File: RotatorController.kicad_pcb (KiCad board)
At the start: 2 copper layers, 117 x 94 mm, 60 parts, among them J1 USB_A, J2 26 VAC, J3 Rotator, K1 G5LE-1, K2 G5LE-1, K3 G5LE-1, Q1 BSS123, Q2 BSS123, Q3 BSS123, SW1 SW_CW, SW2 SW_CCW, U1 Teensy4.0, U3 AP2161W

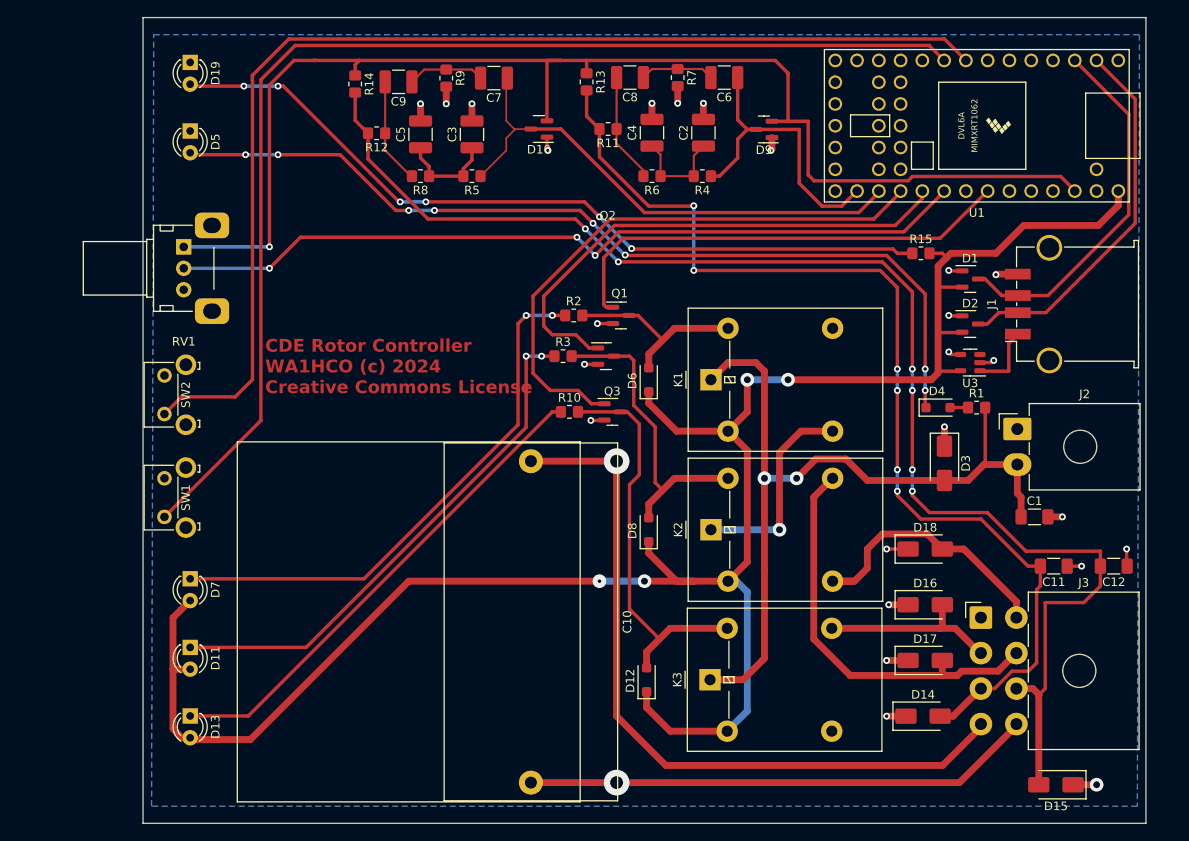
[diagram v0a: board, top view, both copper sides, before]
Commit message: Added files Update board outline based on measurements Moved connectors to new board outline
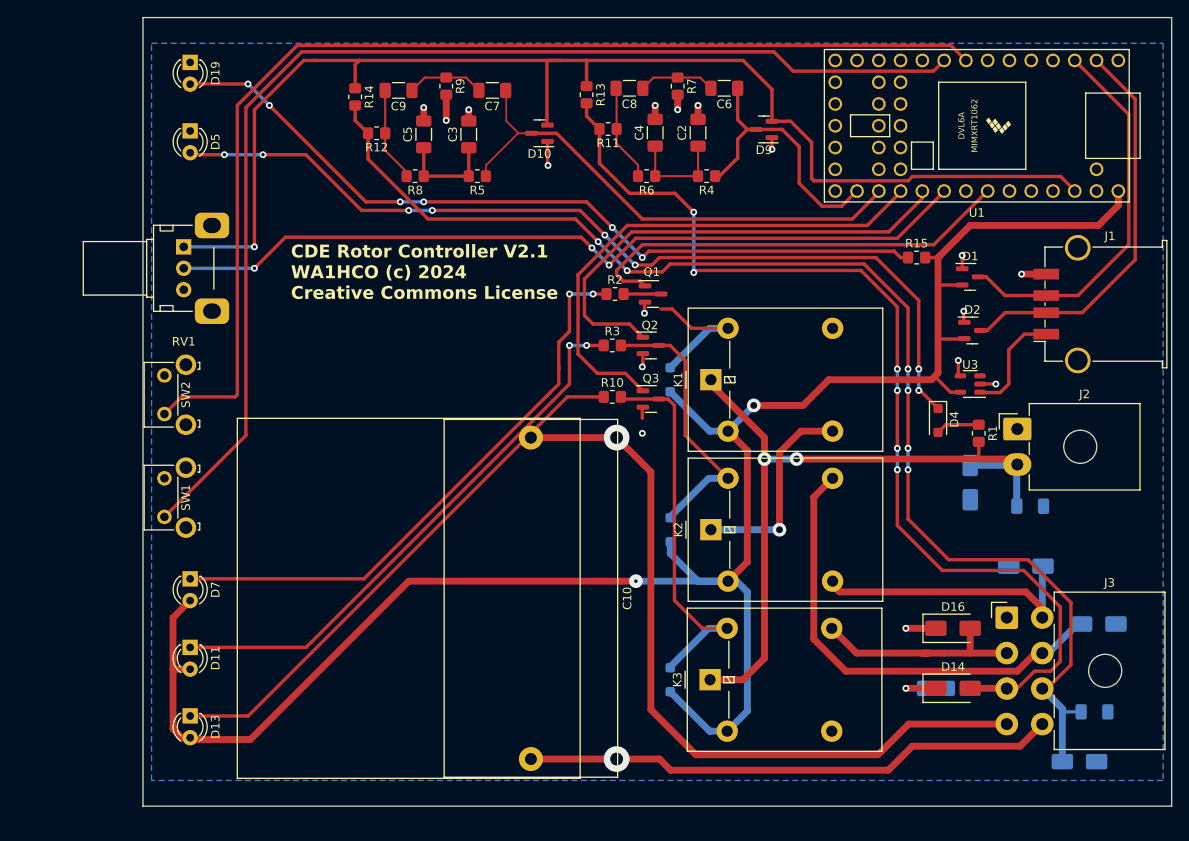
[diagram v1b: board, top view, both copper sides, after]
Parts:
- C1, C11, C12, D12, D15, D17, D18, D3, D6, D8: moved to B.Cu
- C2, C3, C4, C5, C6, C7, C8, C9: footprint Capacitor_SMD:C_1210_3225Metric_Pad1.33x2.70mm_HandSolder -> Capacitor_SMD:C_1206_3216Metric_Pad1.33x1.80mm_HandSolder
- moved D17 20.7 mm to (206.2, 117.8), turned to 180 degrees
- moved C11 19.8 mm to (187.2, 125.2), turned to 0 degrees
- moved C12 17.1 mm to (205.8, 128.0)
- moved D18 11.9 mm to (197.8, 111.0)
- moved R3 5.88 mm to (149.5, 85.2)
- moved R2 5.42 mm to (149.8, 79.2)
- moved Q2 5.40 mm to (154.0, 85.2)
- moved R10 5.30 mm to (149.5, 91.2)
- moved D14 4.78 mm to (189.2, 125.2)
- moved Q3 4.74 mm to (154.0, 91.5)
- moved Q1 4.51 mm to (154.2, 79.2)
- moved D16 4.26 mm to (189.2, 118.2)
- moved D15 3.85 mm to (204.0, 133.8)
- moved D3 3.75 mm to (191.2, 101.2), turned to 90 degrees
- moved J1 3.31 mm to (206.5, 80.4)
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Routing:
- net /Wiper-: track 162.5 -> 148.9 mm
- net GND: track 48.7 -> 35.8 mm, vias 25 -> 18
- net /26VAC: track 94.0 -> 84.7 mm
- net /Right: track 47.9 -> 54.7 mm
- net /Brk_Ctl: track 66.9 -> 60.4 mm
- net /+5V: track 240.5 -> 234.3 mm, vias 4 -> 2
- net Net-(D13-K): track 57.9 -> 63.7 mm
- net Net-(J1-VBUS): track 8.14 -> 12.9 mm
- net Net-(D7-K): track 63.4 -> 68.0 mm
- net /Dir_Ctl: track 61.1 -> 56.7 mm
- net /Brake: track 21.2 -> 25.4 mm
- net Net-(D11-K): track 61.4 -> 65.5 mm
- net /Wiper+: track 124.3 -> 120.3 mm
- net Net-(D8-A): track 36.1 -> 32.8 mm
- net Net-(D4-A): track 2.10 -> 5.12 mm
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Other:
- board size 117 x 94 mm -> 120 x 92 mm
- board text added: "CDE Rotor Controller V2.1 WA1HCO (c) 2024 Creative Commons License"
- board text removed: "CDE Rotor Controller WA1HCO (c) 2024 Creative Commons License"

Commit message: Moved Teensy into position, adjusted related traces
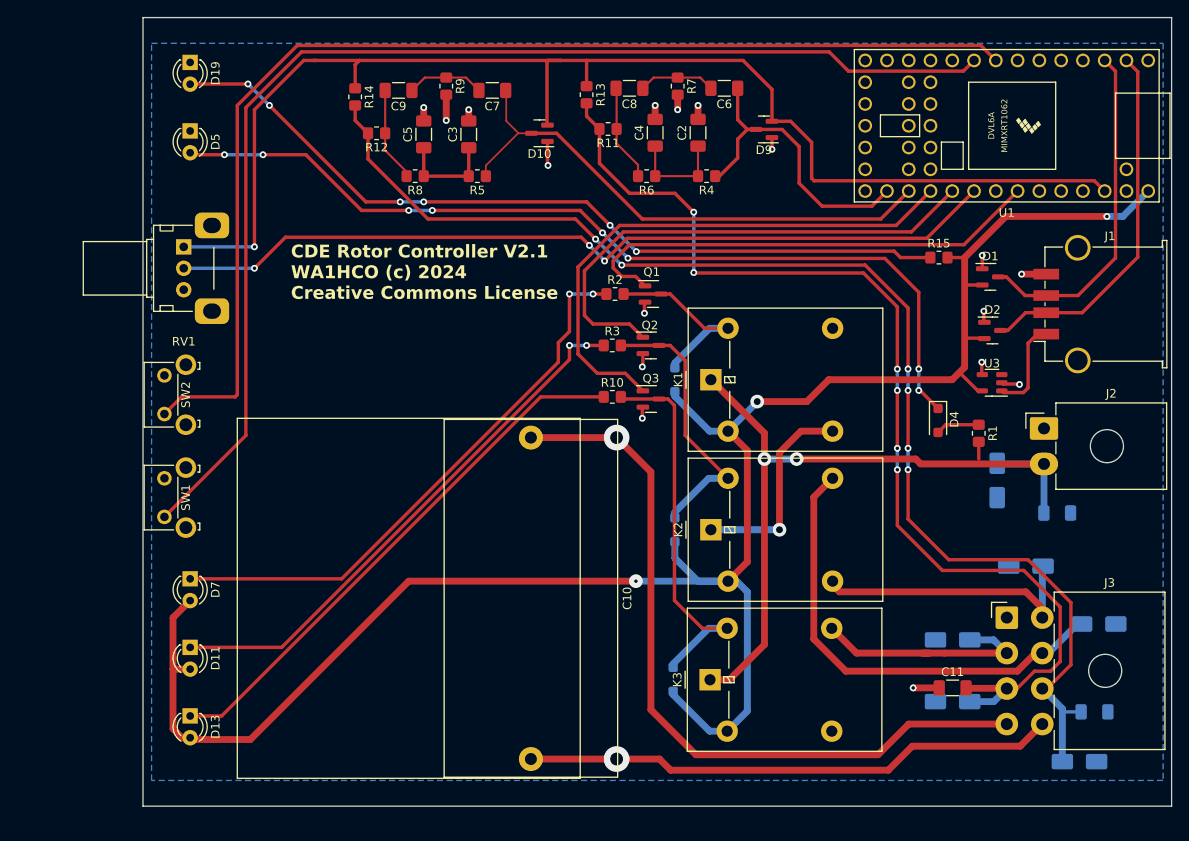
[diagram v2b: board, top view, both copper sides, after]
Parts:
- C11: moved to F.Cu
- D14, D16: moved to B.Cu
- moved U1 3.49 mm to (195.5, 59.6)
- moved C1 3.25 mm to (201.4, 104.8)
- moved D3 3.16 mm to (194.4, 101.0)
- moved J2 3.11 mm to (199.9, 94.9)
- moved R15 2.60 mm to (187.6, 75.0)
- moved U3 2.55 mm to (193.8, 89.6)
- moved D1 2.34 mm to (193.6, 77.2)
- moved D2 2.34 mm to (193.8, 83.5)
- moved C11 1.95 mm to (189.2, 125.2)
- moved D14 1.55 mm to (189.2, 126.8)
- moved D16 1.35 mm to (189.2, 119.6)
- moved D6 0.55 mm to (156.8, 89.2)
- moved D8 0.55 mm to (156.8, 106.8)
- moved D12 0.35 mm to (156.6, 124.2)
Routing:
- net /Wiper+: track 120.3 -> 125.5 mm
- net /Ctlr_Tx: track 45.0 -> 40.0 mm
- net /Mot_Ctl: track 51.7 -> 56.2 mm
- net GND: track 35.8 -> 31.6 mm, vias 18 -> 17
- net /Brk_Ctl: track 60.4 -> 64.3 mm
- net /Ctlr_Rx: track 46.6 -> 43.1 mm
- net /Flt_W+: track 32.3 -> 35.8 mm
- net /CW: track 137.3 -> 140.8 mm
- net /CCW: track 131.8 -> 135.3 mm
- net /Dir_Ctl: track 56.7 -> 59.8 mm
- net /Hdg: track 95.2 -> 98.3 mm
- net /3V3: track 149.7 -> 152.7 mm
- net /26VAC: track 84.7 -> 87.6 mm
- net /Flt_W-: track 60.5 -> 63.2 mm
- net /Brake: track 25.4 -> 27.4 mm
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
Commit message: Mid layout of smaller pcb with separately mounted cap still need to assign cap connector Added 4 high light pipe and 0805 LEDs, need to create footprint
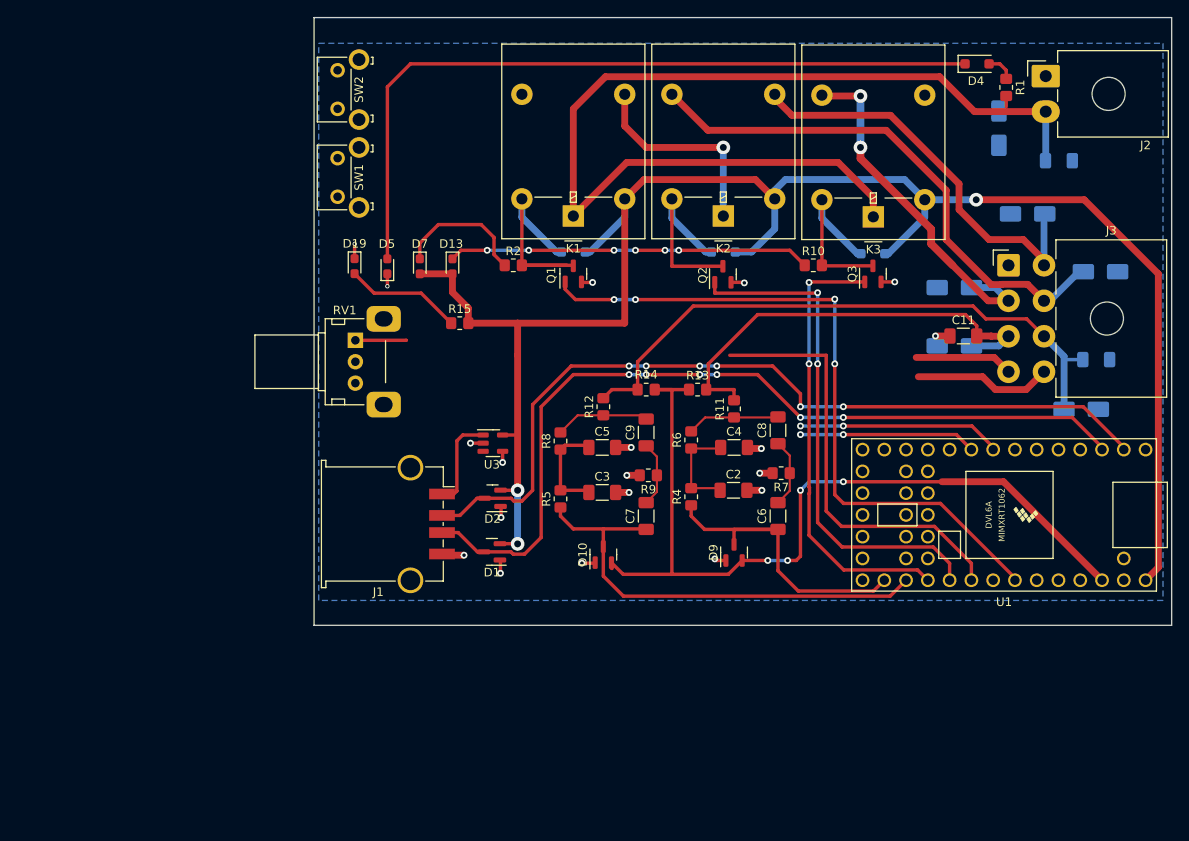
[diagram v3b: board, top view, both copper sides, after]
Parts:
- removed C10: 100 uFd, Capacitor_THT:C_Rect_L41.5mm_W20.0mm_P37.50mm_MKS4
- removed D11: IR204A, LED_THT:LED_D3.0mm_IRBlack
- removed R3: 560, Resistor_SMD:R_0805_2012Metric_Pad1.20x1.40mm_HandSolder
- D13: value IR204A -> Brake; footprint LED_THT:LED_D3.0mm_IRBlack -> LED_SMD:LED_0603_1608Metric_Pad1.05x0.95mm_HandSolder
- D19: value IR204A -> 5V; footprint LED_THT:LED_D3.0mm_IRBlack -> LED_SMD:LED_0603_1608Metric_Pad1.05x0.95mm_HandSolder
- D5: value IR204A -> 26VAC; footprint LED_THT:LED_D3.0mm_IRBlack -> LED_SMD:LED_0603_1608Metric_Pad1.05x0.95mm_HandSolder
- D7: value IR204A -> Motor; footprint LED_THT:LED_D3.0mm_IRBlack -> LED_SMD:LED_0603_1608Metric_Pad1.05x0.95mm_HandSolder
- moved J1 87.1 mm to (123.2, 106.1), turned to -90 degrees
- moved D1 66.4 mm to (135.4, 109.3), turned to 180 degrees
- moved D2 61.5 mm to (135.5, 103.1), turned to 180 degrees
- moved D13 60.7 mm to (130.9, 76.0)
- moved U3 58.7 mm to (135.6, 96.7), turned to 0 degrees
- moved K3 57.3 mm to (179.9, 70.2), turned to 180 degrees
- moved R15 56.4 mm to (131.7, 82.7)
- moved D12 54.8 mm to (179.9, 74.5), turned to 180 degrees
- moved C7 52.8 mm to (153.4, 105.2), turned to 90 degrees
- moved R9 51.2 mm to (153.7, 100.4), turned to 180 degrees
- moved C6 50.3 mm to (168.8, 105.2), turned to 90 degrees
- moved D10 49.7 mm to (148.4, 109.7), turned to 90 degrees
- moved D9 49.5 mm to (163.7, 109.4), turned to 90 degrees
- moved C9 49.3 mm to (153.4, 95.4), turned to 90 degrees
- moved R14 48.2 mm to (153.4, 90.4), turned to 180 degrees
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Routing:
- net /CW: track 140.8 -> 20.7 mm, vias 0 -> 2
- net /CCW: track 135.3 -> 23.8 mm, vias 0 -> 2
- net Net-(D19-A): track 94.8 -> 13.7 mm, vias 6 -> 0
- net /Wiper-: track 148.2 -> 70.9 mm, vias 6 -> 0
- net /Cap1: track 88.6 -> 11.5 mm, vias 1 -> 0
- net /Wiper+: track 125.5 -> 51.4 mm, vias 6 -> 0
- net Net-(D11-K): track 63.8 -> 0.00 mm, vias 2 -> 0
- net /Ctlr_Tx: track 40.0 -> 99.4 mm, vias 0 -> 6
- net /Ctlr_Rx: track 43.1 -> 98.0 mm, vias 0 -> 6
- net Net-(D7-K): track 66.2 -> 15.8 mm, vias 2 -> 0
- net /Hdg: track 98.3 -> 50.9 mm, vias 3 -> 0
- net /3V3: track 152.7 -> 106.0 mm, vias 1 -> 4
- net /Cap2: track 62.4 -> 16.1 mm, vias 1 -> 0
- net /26VAC: track 87.6 -> 124.9 mm, vias 2 -> 0
- net /+5V: track 234.7 -> 207.7 mm
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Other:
- board size 120 x 92 mm -> 100 x 70.9 mm

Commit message: Added light pipe footprint Completed layout and deisgn rule check
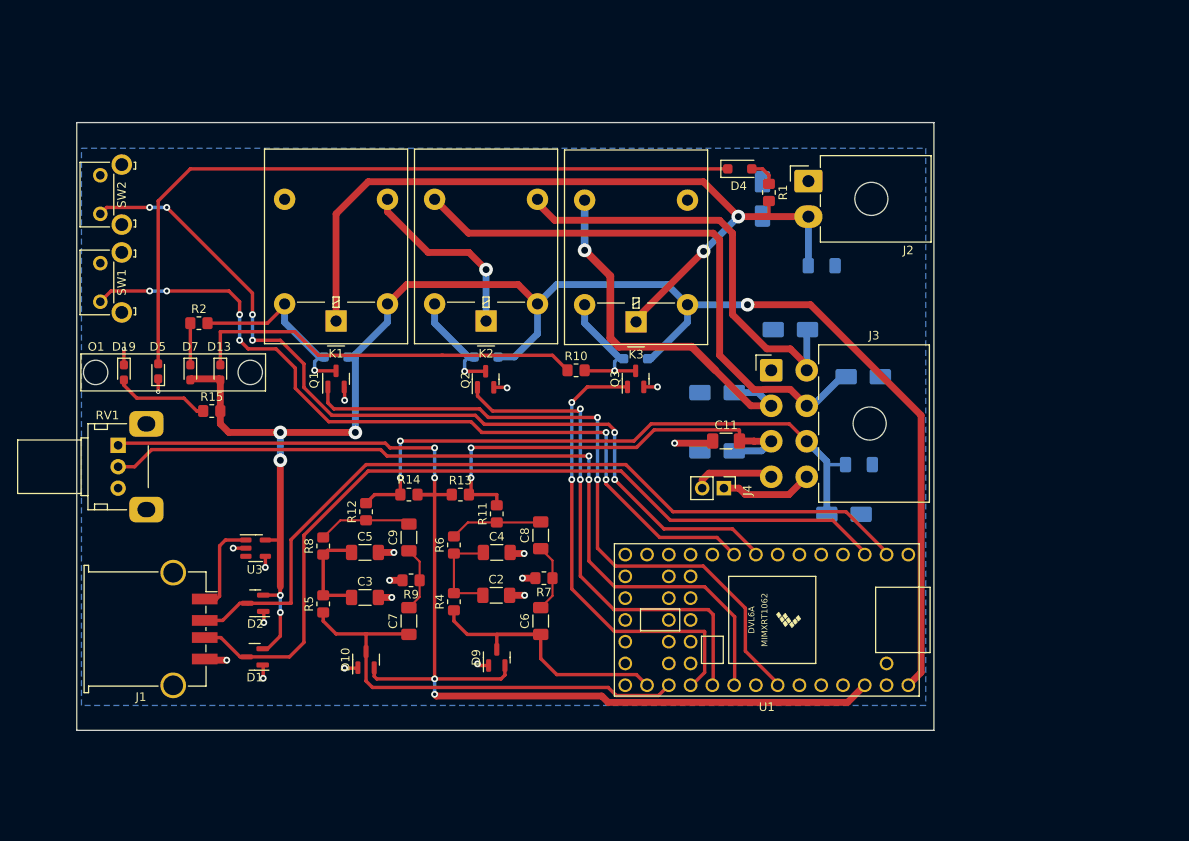
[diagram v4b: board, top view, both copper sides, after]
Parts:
- added J4: Motor Cap, Connector_PinHeader_2.54mm:PinHeader_1x02_P2.54mm_Vertical, F.Cu at (162.5, 101.9)
- added O1: ~, Lightpipe:LP4-EP, F.Cu at (89.2, 88.4)
- moved R2 37.3 mm to (101.3, 82.7)
- moved D18 30.8 mm to (170.3, 83.4)
- moved R15 30.7 mm to (102.8, 92.9)
- moved D4 30.3 mm to (164.4, 64.7)
- moved SW2 30.3 mm to (89.8, 69.9)
- moved RV1 30.3 mm to (91.8, 96.9)
- moved SW1 30.3 mm to (89.8, 80.2)
- moved U3 30.3 mm to (107.9, 108.9)
- moved C1 30.3 mm to (173.9, 76.0)
- moved C11 30.3 mm to (162.8, 96.4)
- moved C12 30.3 mm to (178.3, 99.2)
- moved C2 30.3 mm to (136.0, 114.4)
- moved C3 30.3 mm to (120.6, 114.7)
- moved C4 30.3 mm to (136.0, 109.4)
- moved C5 30.3 mm to (120.6, 109.4)
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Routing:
- net /CCW: track 23.8 -> 101.9 mm, vias 2 -> 6
- net /CW: track 20.7 -> 94.7 mm, vias 2 -> 6
- net /Hdg: track 50.9 -> 96.0 mm, vias 0 -> 2
- net /3V3: track 106.0 -> 141.5 mm
- net /26VAC: track 124.9 -> 101.1 mm, vias 0 -> 2
- net /+5V: track 207.7 -> 194.9 mm, vias 3 -> 6
- net Net-(D7-K): track 15.8 -> 4.88 mm
- net Net-(D8-A): track 22.3 -> 12.8 mm, vias 0 -> 1
- net Net-(D12-A): track 22.0 -> 16.3 mm, vias 0 -> 1
- net /Cap2: track 16.1 -> 10.8 mm
- net Net-(D6-A): track 27.5 -> 22.8 mm, vias 0 -> 1
- net /Right: track 62.8 -> 67.3 mm
- net Net-(D13-K): track 42.2 -> 46.4 mm, vias 6 -> 0
- net GND: track 30.3 -> 33.7 mm
- net /Left: track 47.6 -> 50.2 mm
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
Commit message: Simplified symbol and footprint for Teensy4.0 to remove unused pins Corrected error where footprints reverted to through-hole (mystery)
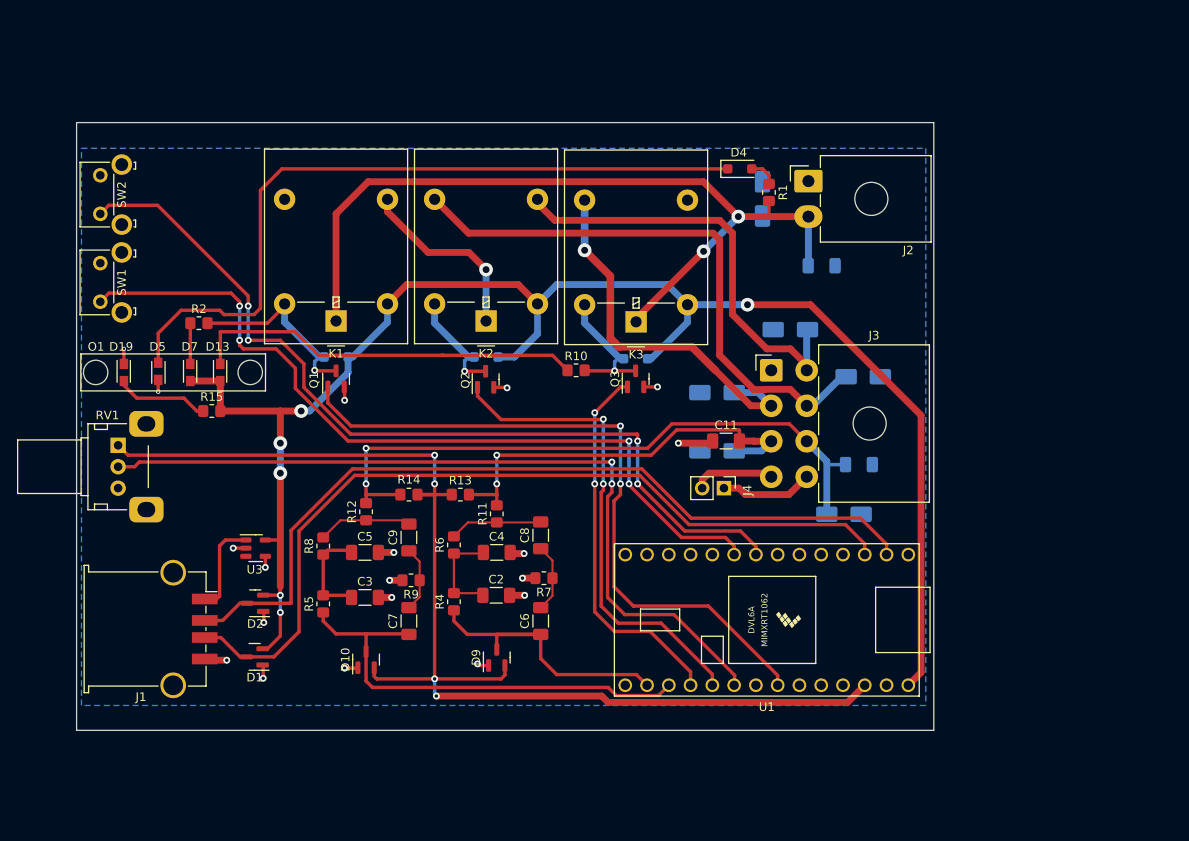
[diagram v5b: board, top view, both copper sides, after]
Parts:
- D13, D19, D5, D7: footprint LED_SMD:LED_0603_1608Metric_Pad1.05x0.95mm_HandSolder -> LED_SMD:LED_miniPLCC_2315_Handsoldering
- U1: footprint Teensy:Teensy40 -> Teensy:Teensy40_Simple
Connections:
- U1 pad 1: GND -> /Ctlr_Tx
- U1 pad 14: unconnected-(U1-12_MISO_MQSL-Pad14) -> /Flt_W+
- U1 pad 15: unconnected-(U1-VBAT-Pad15) -> /Flt_W-
- U1 pad 16: unconnected-(U1-3V3-Pad16) -> /Brk_Ctl
- U1 pad 17: GND -> /Dir_Ctl
- U1 pad 18: unconnected-(U1-PROGRAM-Pad18) -> /Hdg
- U1 pad 2: /Ctlr_Rx -> unconnected-(U1-2_OUT2-Pad2)
- U1 pad 20: unconnected-(U1-13_SCK_CRX1_LED-Pad20) -> /Mot_Ctl
- U1 pad 21: /Flt_W+ -> unconnected-(U1-21_A7_RX5_BCLK1-Pad21)
- U1 pad 22: /Flt_W- -> unconnected-(U1-22_A8_CTX1-Pad22)
- U1 pad 23: /Brk_Ctl -> unconnected-(U1-23_A9_CRX1_MCLK1-Pad23)
- U1 pad 3: /Ctlr_Tx -> unconnected-(U1-3_LRCLK2-Pad3)
- U1 pad 6: unconnected-(U1-4_BCLK2-Pad6) -> /CCW
- U1 pad 7: unconnected-(U1-5_IN2-Pad7) -> /CW
- U1 pad 8: /CCW -> unconnected-(U1-8_TX2_IN1-Pad8)
- U1 pad 9: /CW -> unconnected-(U1-9_OUT1C-Pad9)
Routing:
- net /Brk_Ctl: track 53.6 -> 43.9 mm
- net /+5V: track 194.9 -> 189.4 mm
- net /Wiper-: track 71.4 -> 75.5 mm
- net /Wiper+: track 51.9 -> 48.6 mm
- net /Dir_Ctl: track 59.0 -> 56.3 mm
- net /Hdg: track 96.0 -> 93.6 mm
- net /Ctlr_Rx: track 96.0 -> 96.8 mm
- net /Mot_Ctl: track 80.2 -> 81.0 mm
- net /3V3: track 141.5 -> 140.8 mm
- net Net-(D4-K): track 87.0 -> 86.4 mm
- net /CCW: track 101.9 -> 102.3 mm, vias 6 -> 4
- net /CW: track 94.7 -> 94.9 mm, vias 6 -> 4
